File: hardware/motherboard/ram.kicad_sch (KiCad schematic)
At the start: 5 parts, among them U401 K4E6E304ED-EGCG

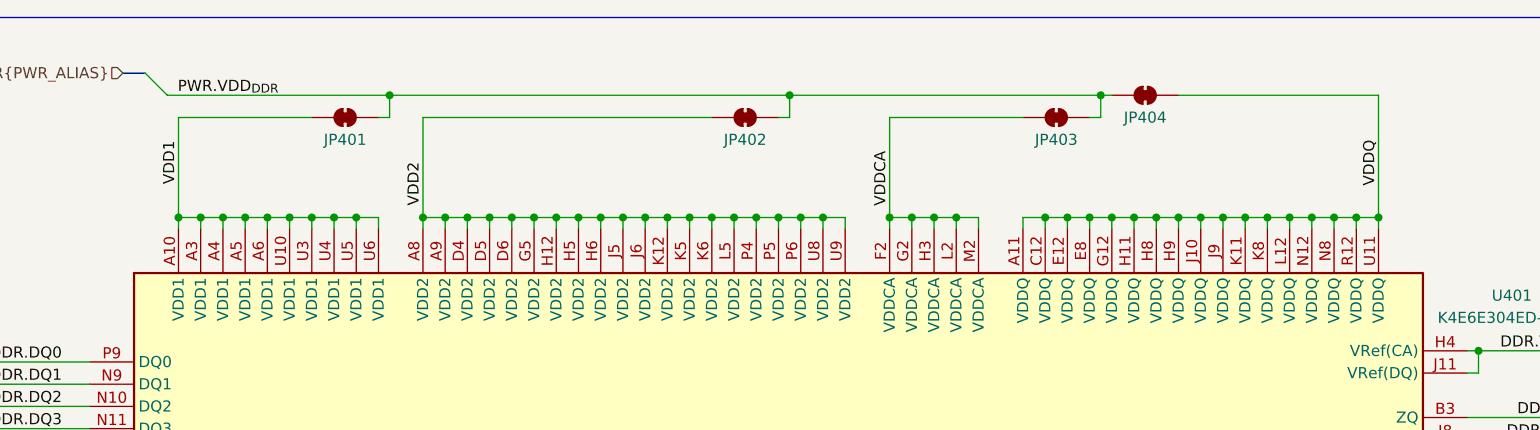
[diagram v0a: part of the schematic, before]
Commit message: Start routing RAM, add more docs
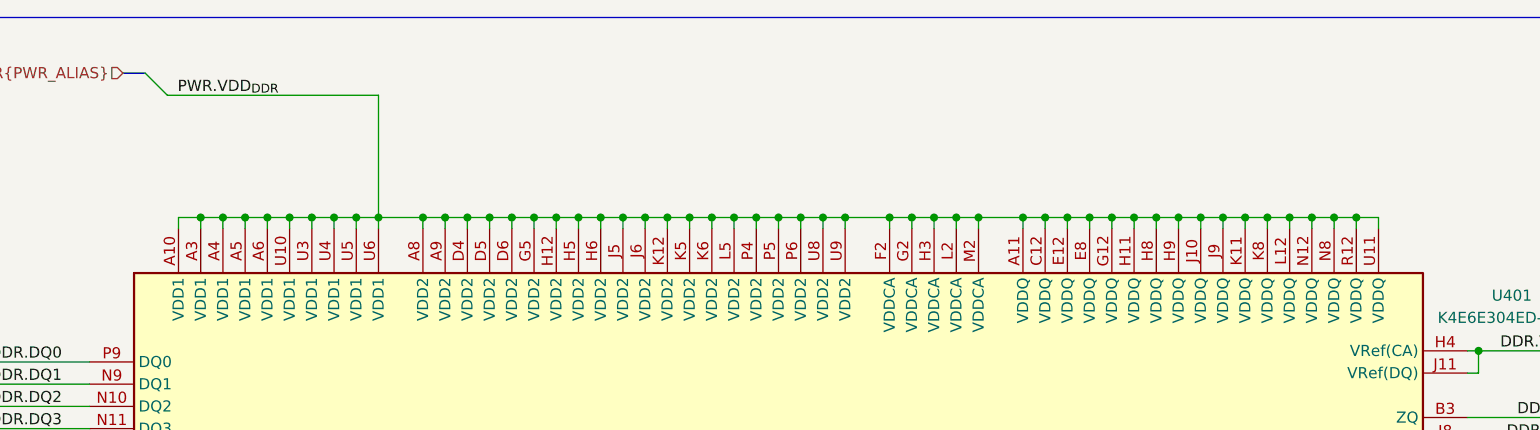
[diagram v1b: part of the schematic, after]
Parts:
- removed JP401, JP402, JP403, JP404: SolderJumper_2_Bridged, symbol Jumper:SolderJumper_2_Bridged
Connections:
- net VDD1 is gone; now on net PWR.VDD_{DDR}: U401.A10 (VDD1), U401.A3 (VDD1), U401.A4 (VDD1), U401.A5 (VDD1), U401.A6 (VDD1), U401.U10 (VDD1), U401.U3 (VDD1), U401.U4 (VDD1), U401.U5 (VDD1), U401.U6 (VDD1)
- net VDD2 is gone; now on net PWR.VDD_{DDR}: U401.A8 (VDD2), U401.A9 (VDD2), U401.D4 (VDD2), U401.D5 (VDD2), U401.D6 (VDD2), U401.G5 (VDD2), U401.H12 (VDD2), U401.H5 (VDD2), U401.H6 (VDD2), U401.J5 (VDD2), U401.J6 (VDD2), U401.K12 (VDD2), U401.K5 (VDD2), U401.K6 (VDD2), U401.L5 (VDD2), U401.P4 (VDD2), U401.P5 (VDD2), U401.P6 (VDD2), U401.U8 (VDD2), U401.U9 (VDD2)
- net VDDCA is gone; now on net PWR.VDD_{DDR}: U401.F2 (VDDCA), U401.G2 (VDDCA), U401.H3 (VDDCA), U401.L2 (VDDCA), U401.M2 (VDDCA)
- net VDDQ is gone; now on net PWR.VDD_{DDR}: U401.A11 (VDDQ), U401.C12 (VDDQ), U401.E12 (VDDQ), U401.E8 (VDDQ), U401.G12 (VDDQ), U401.H11 (VDDQ), U401.H8 (VDDQ), U401.H9 (VDDQ), U401.J10 (VDDQ), U401.J9 (VDDQ), U401.K11 (VDDQ), U401.K8 (VDDQ), U401.L12 (VDDQ), U401.N12 (VDDQ), U401.N8 (VDDQ), U401.R12 (VDDQ), U401.U11 (VDDQ)
